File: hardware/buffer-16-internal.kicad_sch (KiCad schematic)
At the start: 6 parts, among them U4 74LVC8T245, U5 74LVC8T245

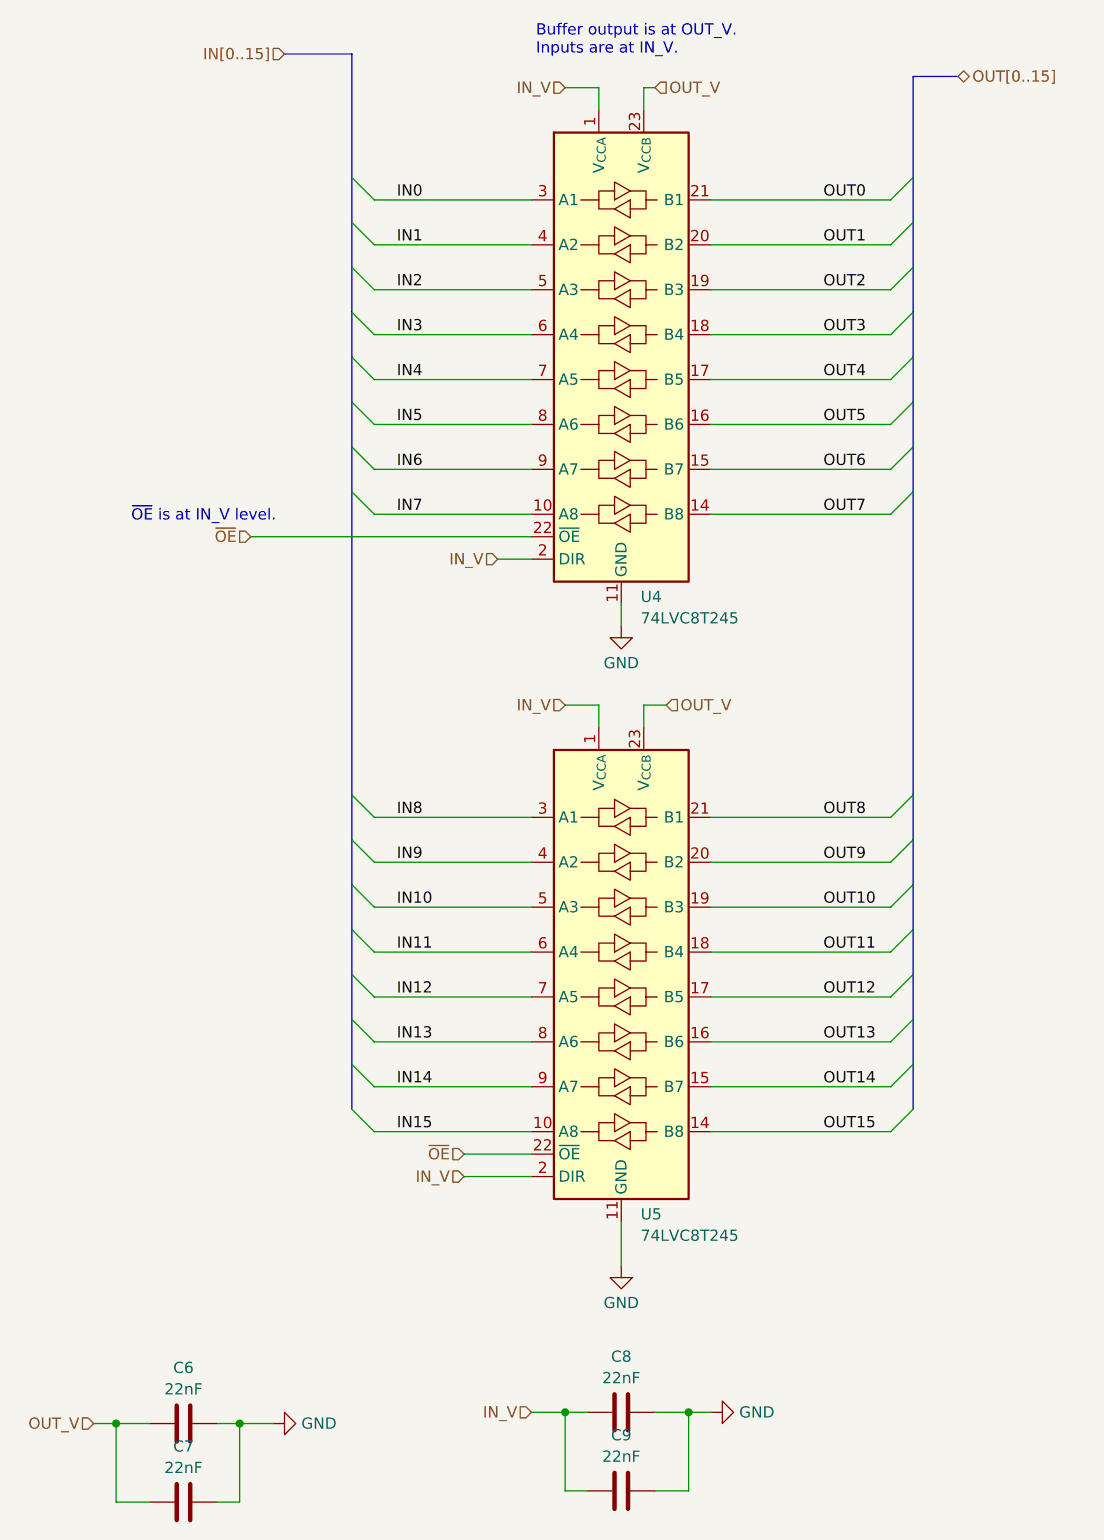
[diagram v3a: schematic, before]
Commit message: Update KiCad to 9.0
Open and save every schematic and board file without changing anything
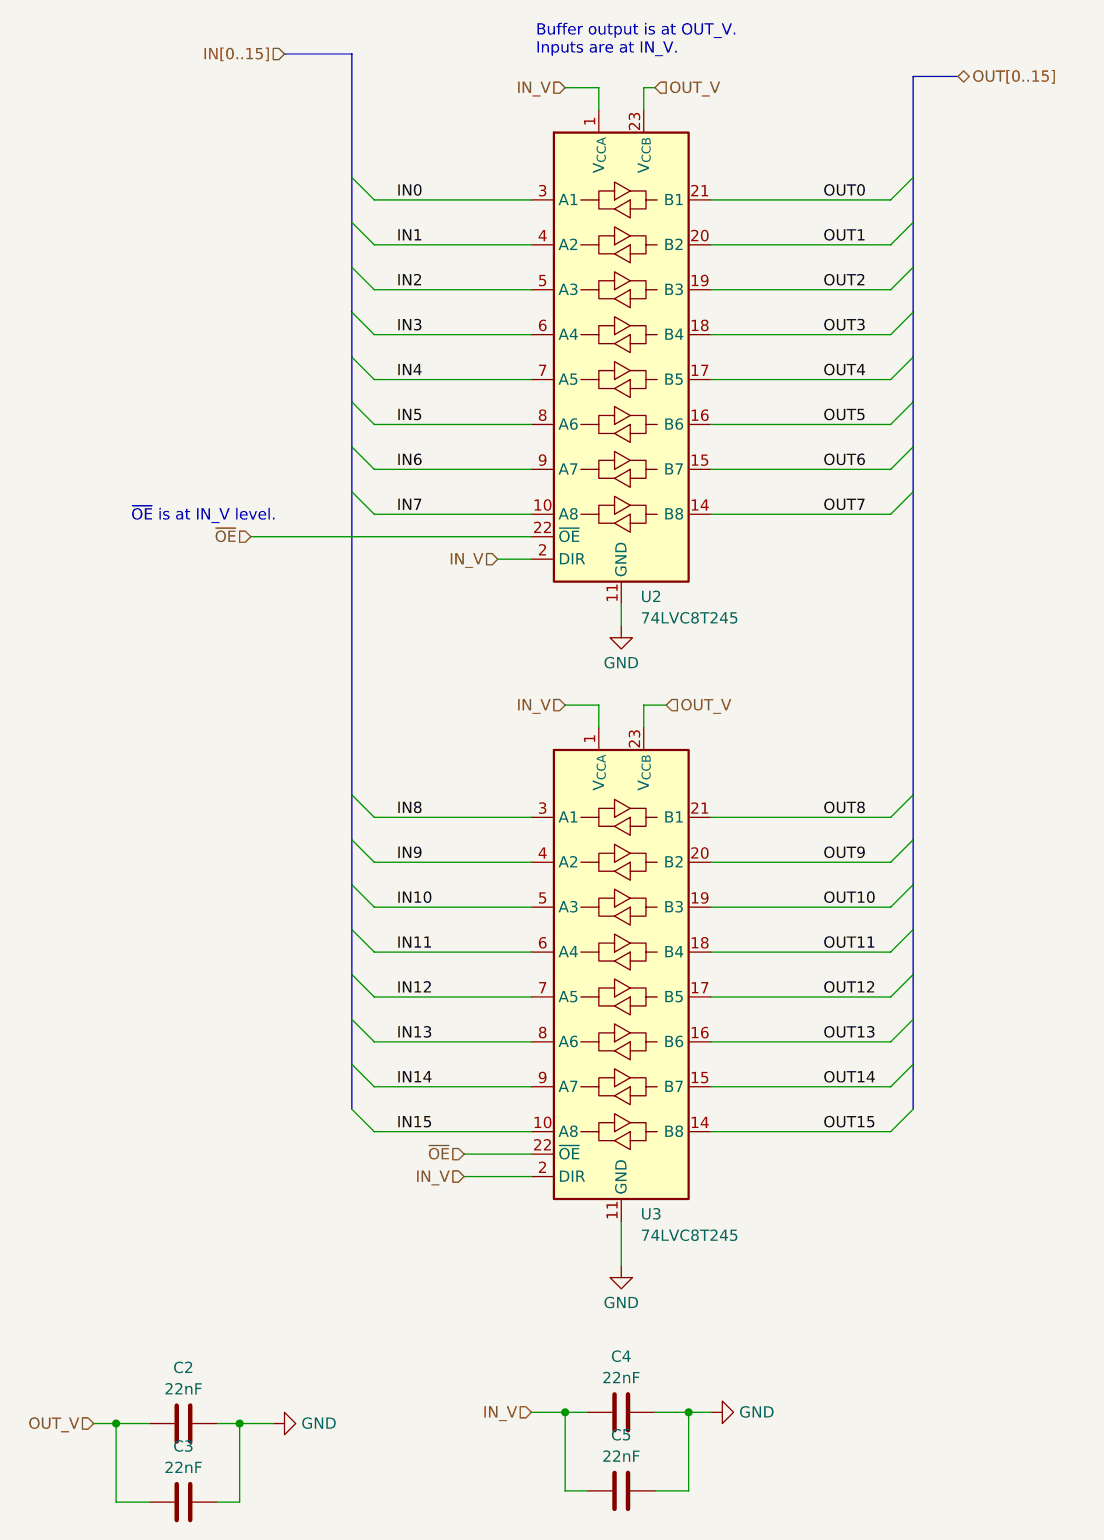
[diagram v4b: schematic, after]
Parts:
- renumbered C6 to C2, C7 to C3, C8 to C4, C9 to C5, U4 to U2, U5 to U3
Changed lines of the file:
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@@
 (kicad_sch
-	(version 20231120)
+	(version 20250114)
 	(generator "eeschema")
-	(generator_version "8.0")
+	(generator_version "9.0")
 	(paper "A4")
 	(title_block
 		(title "16-bit buffer connected to buses")
+	)
+	(text "Buffer output is at OUT_V.\nInputs are at IN_V."
+		(exclude_from_sim no)
+		(at 117.348 21.336 0)
+		(effects
+			(font
+				(size 1.27 1.27)
+			)
+			(justify left)
+		)
+	)
+	(text "~{OE} is at IN_V level."
+		(exclude_from_sim no)
+		(at 79.756 75.184 0)
+		(effects
+			(font
+				(size 1.27 1.27)
+			)
+		)
 	)
 	(junction
@@
 		)
 	)
-	(text "Buffer output is at OUT_V.\nInputs are at IN_V."
-		(exclude_from_sim no)
-		(at 117.348 21.336 0)
-		(effects
-			(font
-				(size 1.27 1.27)
-			)
-			(justify left)
-		)
-	)
-	(text "~{OE} is at IN_V level."
-		(exclude_from_sim no)
-		(at 79.756 75.184 0)
-		(effects
-			(font
-				(size 1.27 1.27)
-			)
-		)
-	)
 	(label "OUT4"
 		(at 149.86 59.69 0)
-		(fields_autoplaced yes)
 		(effects
 			(font
@@
 	(label "IN11"
 		(at 101.6 124.46 0)
-		(fields_autoplaced yes)
 		(effects
 			(font
@@
 	(label "OUT13"
 		(at 149.86 134.62 0)
-		(fields_autoplaced yes)
 		(effects
 			(font
@@
 	(label "OUT15"
 		(at 149.86 144.78 0)
-		(fields_autoplaced yes)
 		(effects
 			(font
@@
 	(label "IN8"
 		(at 101.6 109.22 0)
-		(fields_autoplaced yes)
 		(effects
 			(font
@@
 	(label "IN13"
 		(at 101.6 134.62 0)
-		(fields_autoplaced yes)
 		(effects
 			(font
@@
 	(label "IN0"
 		(at 101.6 39.37 0)
-		(fields_autoplaced yes)
 		(effects
 			(font
@@
 	(label "OUT12"
 		(at 149.86 129.54 0)
-		(fields_autoplaced yes)
 		(effects
 			(font
@@
 	(label "IN9"
 		(at 101.6 114.3 0)
-		(fields_autoplaced yes)
 		(effects
 			(font
@@
 	(label "OUT2"
 		(at 149.86 49.53 0)
-		(fields_autoplaced yes)
 		(effects
 			(font
@@
 	(label "IN12"
 		(at 101.6 129.54 0)
-		(fields_autoplaced yes)
 		(effects
 			(font
@@
 	(label "OUT14"
 		(at 149.86 139.7 0)
-		(fields_autoplaced yes)
 		(effects
 			(font
@@
 	(label "OUT1"
 		(at 149.86 44.45 0)
-		(fields_autoplaced yes)
 		(effects
 			(font
@@
 	(label "OUT6"
 		(at 149.86 69.85 0)
-		(fields_autoplaced yes)
 		(effects
 			(font
@@
 	(label "IN10"
 		(at 101.6 119.38 0)
-		(fields_autoplaced yes)
 		(effects
 			(font
@@
 	(label "OUT7"
 		(at 149.86 74.93 0)
-		(fields_autoplaced yes)
 		(effects
 			(font
@@
 	(label "OUT9"
 		(at 149.86 114.3 0)
-		(fields_autoplaced yes)
 		(effects
 			(font
@@
 	(label "IN1"
 		(at 101.6 44.45 0)
-		(fields_autoplaced yes)
 		(effects
 			(font
@@
 	(label "IN14"
 		(at 101.6 139.7 0)
-		(fields_autoplaced yes)
 		(effects
 			(font
@@
 	(label "OUT10"
 		(at 149.86 119.38 0)
-		(fields_autoplaced yes)
 		(effects
 			(font
@@
 	(label "OUT8"
 		(at 149.86 109.22 0)
-		(fields_autoplaced yes)
 		(effects
 			(font
@@
 	(label "IN6"
 		(at 101.6 69.85 0)
-		(fields_autoplaced yes)
 		(effects
 			(font
@@
 	(label "IN7"
 		(at 101.6 74.93 0)
-		(fields_autoplaced yes)
 		(effects
 			(font
@@
 	(label "IN3"
 		(at 101.6 54.61 0)
-		(fields_autoplaced yes)
 		(effects
 			(font
@@
 	(label "IN5"
 		(at 101.6 64.77 0)
-		(fields_autoplaced yes)
 		(effects
 			(font
@@
 	(label "OUT0"
 		(at 149.86 39.37 0)
-		(fields_autoplaced yes)
 		(effects
 			(font
@@
 	(label "IN15"
 		(at 101.6 144.78 0)
-		(fields_autoplaced yes)
 		(effects
 			(font
@@
 	(label "IN2"
 		(at 101.6 49.53 0)
-		(fields_autoplaced yes)
 		(effects
 			(font
@@
 	(label "OUT3"
 		(at 149.86 54.61 0)
-		(fields_autoplaced yes)
 		(effects
 			(font
@@
 	(label "OUT11"
 		(at 149.86 124.46 0)
-		(fields_autoplaced yes)
 		(effects
 			(font
@@
 	(label "OUT5"
 		(at 149.86 64.77 0)
-		(fields_autoplaced yes)
 		(effects
 			(font
@@
 	(label "IN4"
 		(at 101.6 59.69 0)
-		(fields_autoplaced yes)
 		(effects
 			(font
@@
 		(shape input)
 		(at 67.31 177.8 180)
-		(fields_autoplaced yes)
 		(effects
 			(font
@@
 		(shape input)
 		(at 88.9 22.86 180)
-		(fields_autoplaced yes)
 		(effects
 			(font
@@
 		(shape tri_state)
 		(at 165.1 25.4 0)
-		(fields_autoplaced yes)
 		(effects
 			(font
@@
 		(shape input)
 		(at 130.81 26.67 0)
-		(fields_autoplaced yes)
 		(effects
 			(font
@@
 		(shape input)
 		(at 120.65 96.52 180)
-		(fields_autoplaced yes)
 		(effects
 			(font
@@
 		(shape input)
 		(at 109.22 149.86 180)
-		(fields_autoplaced yes)
 		(effects
 			(font
@@
 		(shape input)
 		(at 85.09 77.47 180)
-		(fields_autoplaced yes)
 		(effects
 			(font
@@
 		(shape input)
 		(at 113.03 80.01 180)
-		(fields_autoplaced yes)
 		(effects
 			(font
@@
 		(shape input)
 		(at 109.22 147.32 180)
-		(fields_autoplaced yes)
 		(effects
 			(font
@@
 		(shape input)
 		(at 132.08 96.52 0)
-		(fields_autoplaced yes)
 		(effects
 			(font
@@
 		(shape input)
 		(at 116.84 176.53 180)
-		(fields_autoplaced yes)
 		(effects
 			(font
@@
 		(shape input)
 		(at 120.65 26.67 180)
-		(fields_autoplaced yes)
 		(effects
 			(font
@@
 		(dnp no)
 		(fields_autoplaced yes)
-		(property "Reference" "U4"
+		(property "Reference" "U2"
 			(at 129.1941 84.2701 0)
 			(effects
@@
 		(dnp no)
 		(fields_autoplaced yes)
-		(property "Reference" "#PWR039"
+		(property "Reference" "#PWR038"
 			(at 127 166.37 0)
 			(effects
@@
 		(dnp no)
 		(fields_autoplaced yes)
-		(property "Reference" "C8"
+		(property "Reference" "C4"
 			(at 127 170.2265 90)
 			(effects
@@
 		(dnp no)
 		(fields_autoplaced yes)
-		(property "Reference" "#PWR041"
+		(property "Reference" "#PWR040"
 			(at 93.98 177.8 0)
 			(effects
@@
 		(dnp no)
 		(fields_autoplaced yes)
-		(property "Reference" "C7"
+		(property "Reference" "C3"
 			(at 77.47 180.3865 90)
 			(effects
@@
 		(dnp no)
 		(fields_autoplaced yes)
-		(property "Reference" "C6"
+		(property "Reference" "C2"
 			(at 77.47 171.4965 90)
 			(effects
@@
 		(dnp no)
 		(fields_autoplaced yes)
-		(property "Reference" "#PWR043"
+		(property "Reference" "#PWR042"
 			(at 143.51 176.53 0)
 			(effects
@@
 		(dnp no)
 		(fields_autoplaced yes)
-		(property "Reference" "C9"
+		(property "Reference" "C5"
 			(at 127 179.1165 90)
 			(effects
@@
 		(dnp no)
 		(fields_autoplaced yes)
-		(property "Reference" "U5"
+		(property "Reference" "U3"
 			(at 129.1941 154.1201 0)
 			(effects
@@
 		(dnp no)
 		(fields_autoplaced yes)
-		(property "Reference" "#PWR037"
+		(property "Reference" "#PWR036"
 			(at 127 93.98 0)
 			(effects
